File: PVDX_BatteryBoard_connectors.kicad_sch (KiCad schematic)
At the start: 1 part, among them J1 Conn_01x06_Socket

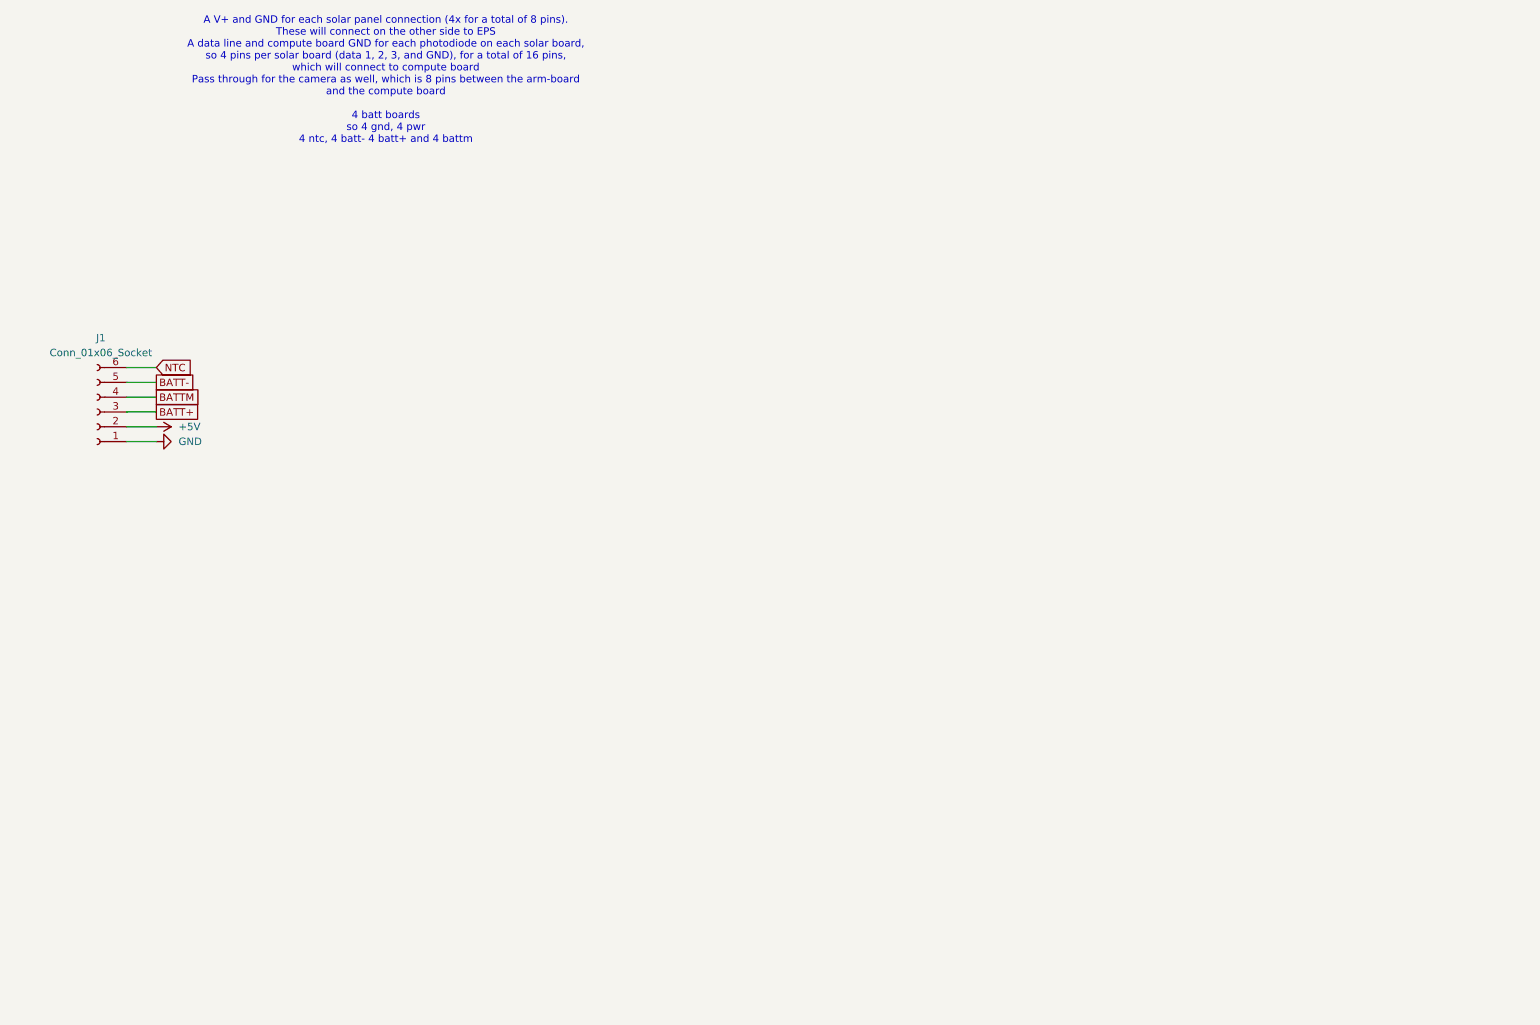
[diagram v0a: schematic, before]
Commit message: Finish battery board schematic (awaiting thermistor part no.)
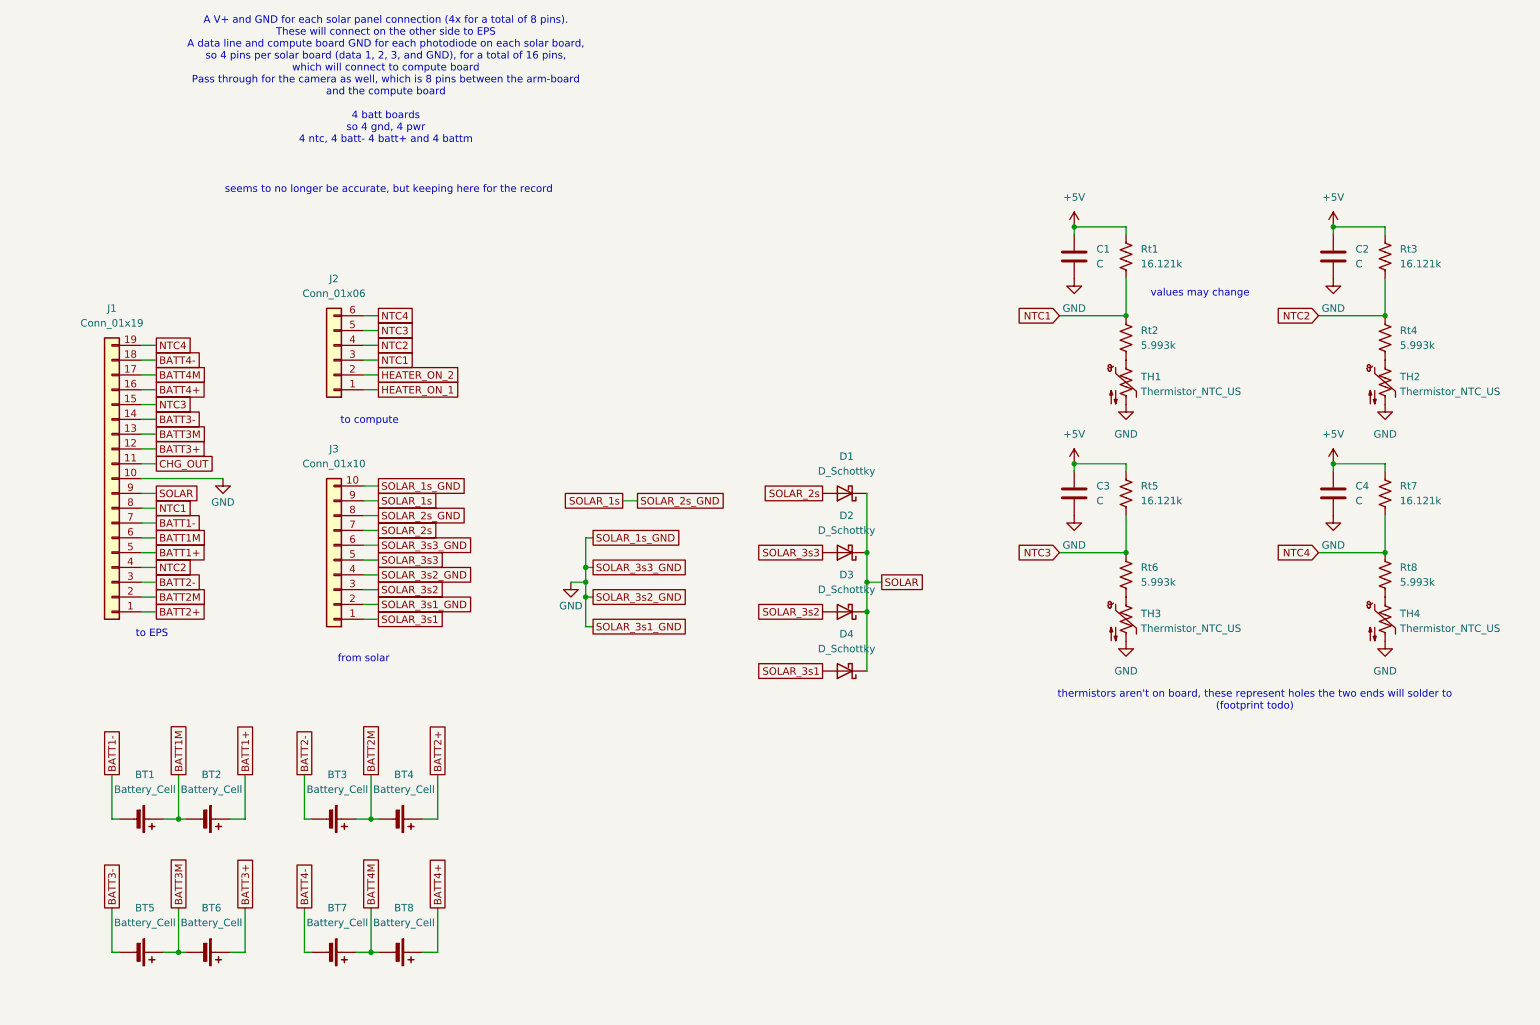
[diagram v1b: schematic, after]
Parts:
- removed J1: Conn_01x06_Socket, symbol Connector:Conn_01x06_Socket
- added BT1, BT2, BT3, BT4, BT5, BT6, BT7, BT8: Battery_Cell, symbol Device:Battery_Cell
- added C1, C2, C3, C4: C, symbol Device:C
- added D1, D2, D3, D4: D_Schottky, Diode_SMD:D_SOD-128, symbol Device:D_Schottky
- added J1: Conn_01x19, Connector_PinHeader_2.54mm:PinHeader_1x19_P2.54mm_Vertical, symbol Connector_Generic:Conn_01x19
- added J2: Conn_01x06, symbol Connector_Generic:Conn_01x06
- added J3: Conn_01x10, symbol Connector_Generic:Conn_01x10
- added Rt1, Rt3, Rt5, Rt7: 16.121k, symbol Device:R_US
- added Rt2, Rt4, Rt6, Rt8: 5.993k, symbol Device:R_US
- added TH1, TH2, TH3, TH4: Thermistor_NTC_US, Thermistor_NXFT15XV103FEAB025:Thermistor_ NXFT15XV103FEAB025, symbol Device:Thermistor_NTC_US
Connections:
- net +5V: now also C1.1, C2.1, C3.1, C4.1, Rt1.1, Rt3.1, Rt5.1, Rt7.1
- net GND: now also C1.2, C2.2, C3.2, C4.2, J1.10 (Pin_10), J3.10 (Pin_10), J3.2 (Pin_2), J3.4 (Pin_4), J3.6 (Pin_6), TH1.2, TH2.2, TH3.2, TH4.2
- new net: Rt4.2, TH2.1
- new net: Rt6.2, TH3.1
- new net: Rt8.2, TH4.1
- new net: Rt2.2, TH1.1
- new net BATT1+: BT2.1 (+), J1.5 (Pin_5)
- new net BATT1-: BT1.2 (-), J1.7 (Pin_7)
- new net BATT1M: BT1.1 (+), BT2.2 (-), J1.6 (Pin_6)
- new net BATT2+: BT4.1 (+), J1.1 (Pin_1)
- new net BATT2-: BT3.2 (-), J1.3 (Pin_3)
- new net BATT2M: BT3.1 (+), BT4.2 (-), J1.2 (Pin_2)
- new net BATT3+: BT6.1 (+), J1.12 (Pin_12)
- new net BATT3-: BT5.2 (-), J1.14 (Pin_14)
- new net BATT3M: BT5.1 (+), BT6.2 (-), J1.13 (Pin_13)
- new net BATT4+: BT8.1 (+), J1.16 (Pin_16)
- new net BATT4-: BT7.2 (-), J1.18 (Pin_18)
- new net BATT4M: BT7.1 (+), BT8.2 (-), J1.17 (Pin_17)
- new net CHG_OUT: J1.11 (Pin_11)
- new net HEATER_ON_1: J2.1 (Pin_1)
- new net HEATER_ON_2: J2.2 (Pin_2)
- new net NTC1: J1.8 (Pin_8), J2.3 (Pin_3), Rt1.2, Rt2.1
- new net NTC2: J1.4 (Pin_4), J2.4 (Pin_4), Rt3.2, Rt4.1
- new net NTC3: J1.15 (Pin_15), J2.5 (Pin_5), Rt5.2, Rt6.1
- new net NTC4: J1.19 (Pin_19), J2.6 (Pin_6), Rt7.2, Rt8.1
- new net SOLAR: D1.1 (K), D2.1 (K), D3.1 (K), D4.1 (K), J1.9 (Pin_9)
- new net SOLAR_1s: J3.8 (Pin_8), J3.9 (Pin_9)
- new net SOLAR_2s: D1.2 (A), J3.7 (Pin_7)
- new net SOLAR_3s1: D4.2 (A), J3.1 (Pin_1)
- new net SOLAR_3s2: D3.2 (A), J3.3 (Pin_3)
- new net SOLAR_3s3: D2.2 (A), J3.5 (Pin_5)
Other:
- note added: "from solar"
- note added: "seems to no longer be accurate, but keeping here for the record"
- note added: "thermistors aren't on board, these represent holes the two ends will solder to (footprint todo)"
- note added: "to EPS"
- note added: "to compute"
- note added: "values may change"

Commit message: Add thermistor & MOSFET parts/values
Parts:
- Rt1, Rt3, Rt5, Rt7: value 16.121k -> 15.8k
- Rt2, Rt4, Rt6, Rt8: value 5.993k -> 5.83k
- TH1, TH2, TH3, TH4: value Thermistor_NTC_US -> GA10K3A1IA
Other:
- note added: "actual desired values: 15.7k, 5.78k values are rounded to ones that actually exist"
- note removed: "values may change"
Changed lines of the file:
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@@
 		)
 	)
-	(text "values may change"
+	(text "actual desired values: 15.7k, 5.78k\nvalues are rounded to ones that actually exist"
 		(exclude_from_sim no)
-		(at 219.71 71.12 0)
+		(at 227.584 48.006 0)
 		(effects
 			(font
@@
 			)
 		)
-		(property "Value" "Thermistor_NTC_US"
+		(property "Value" "GA10K3A1IA"
 			(at 254 87.9474 0)
 			(show_name no)
@@
 			)
 		)
-		(property "Value" "5.993k"
+		(property "Value" "5.83k"
 			(at 209.55 120.6499 0)
 			(show_name no)
@@
 			)
 		)
-		(property "Value" "16.121k"
+		(property "Value" "15.8k"
 			(at 209.55 106.6799 0)
 			(show_name no)
@@
 			)
 		)
-		(property "Value" "5.993k"
+		(property "Value" "5.83k"
 			(at 254 120.6499 0)
 			(show_name no)
@@
 			)
 		)
-		(property "Value" "Thermistor_NTC_US"
+		(property "Value" "GA10K3A1IA"
 			(at 254 128.5874 0)
 			(show_name no)
@@
 			)
 		)
-		(property "Value" "5.993k"
+		(property "Value" "5.83k"
 			(at 254 80.0099 0)
 			(show_name no)
@@
 			)
 		)
-		(property "Value" "Thermistor_NTC_US"
+		(property "Value" "GA10K3A1IA"
 			(at 209.55 128.5874 0)
 			(show_name no)
@@
 			)
 		)
-		(property "Value" "Thermistor_NTC_US"
+		(property "Value" "GA10K3A1IA"
 			(at 209.55 87.9474 0)
 			(show_name no)
@@
 			)
 		)
-		(property "Value" "16.121k"
+		(property "Value" "15.8k"
 			(at 254 106.6799 0)
 			(show_name no)
@@
 			)
 		)
-		(property "Value" "16.121k"
+		(property "Value" "15.8k"
 			(at 254 66.0399 0)
 			(show_name no)
@@
 			)
 		)
-		(property "Value" "16.121k"
+		(property "Value" "15.8k"
 			(at 209.55 66.0399 0)
 			(show_name no)
@@
 			)
 		)
-		(property "Value" "5.993k"
+		(property "Value" "5.83k"
 			(at 209.55 80.0099 0)
 			(show_name no)

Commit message: finished routing
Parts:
- added J10, J4, J6, J8: Conn_01x02_Pin, Connector_PinSocket_2.54mm:PinSocket_1x02_P2.54mm_Vertical, symbol Connector:Conn_01x02_Pin
- added J11, J5, J7, J9: Conn_01x01_Pin, Connector_PinSocket_2.54mm:PinSocket_1x01_P2.54mm_Vertical, symbol Connector:Conn_01x01_Pin
- added J12: Conn_01x02, Connector_PinHeader_2.54mm:PinHeader_1x02_P2.54mm_Vertical, symbol Connector_Generic:Conn_01x02
- C1, C2, C3, C4: value C -> .1u; footprint (none) -> Capacitor_SMD:C_0603_1608Metric
- J2: footprint (none) -> Connector_PinSocket_2.54mm:PinSocket_1x06_P2.54mm_Vertical
- J3: footprint (none) -> Connector_PinSocket_2.54mm:PinSocket_1x10_P2.54mm_Vertical
- Rt1, Rt2, Rt3, Rt4, Rt5, Rt6, Rt7, Rt8: footprint (none) -> Resistor_SMD:R_0603_1608Metric
- TH1, TH2, TH3, TH4: footprint Thermistor_NXFT15XV103FEAB025:Thermistor_ NXFT15XV103FEAB025 -> Connector_PinHeader_2.54mm:PinHeader_1x02_P2.54mm_Vertical
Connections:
- net +5V: now also J12.2 (Pin_2)
- net BATT1+: now also J4.2 (Pin_2)
- net BATT1-: now also J4.1 (Pin_1)
- net BATT1M: now also J5.1 (Pin_1)
- net BATT2+: now also J6.2 (Pin_2)
- net BATT2-: now also J6.1 (Pin_1)
- net BATT2M: now also J7.1 (Pin_1)
- net BATT3+: now also J8.2 (Pin_2)
- net BATT3-: now also J8.1 (Pin_1)
- net BATT3M: now also J9.1 (Pin_1)
- net BATT4+: now also J10.2 (Pin_2)
- net BATT4-: now also J10.1 (Pin_1)
- net BATT4M: now also J11.1 (Pin_1)
- net GND: now also J12.1 (Pin_1)
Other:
- note added: "add 5v and gnd on left side"
- moved on the sheet: BT3, BT4, BT5, BT6, BT7, BT8

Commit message: Add screw holes, make battery pack mid 2 holes
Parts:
- removed J11, J5, J7, J9: Conn_01x01_Pin, Connector_PinSocket_2.54mm:PinSocket_1x01_P2.54mm_Vertical, symbol Connector:Conn_01x01_Pin
- added J11, J5, J7, J9: Conn_01x02_Pin, Connector_PinSocket_2.54mm:PinSocket_1x02_P2.54mm_Vertical, symbol Connector:Conn_01x02_Pin
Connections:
- net BATT1M: now also J5.1 (Pin_1), J5.2 (Pin_2)
- net BATT2M: now also J7.1 (Pin_1), J7.2 (Pin_2)
- net BATT3M: now also J9.1 (Pin_1), J9.2 (Pin_2)
- net BATT4M: now also J11.1 (Pin_1), J11.2 (Pin_2)
